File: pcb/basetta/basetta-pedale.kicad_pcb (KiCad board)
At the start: 2 copper layers, 100 x 72 mm, 33 parts, among them J1 J1, J10 J10, J2 J2, J3 J3, J4 J4, J5 J5, J6 J6, J7 J7, J8 J8, J9 J9, U1 XIAO ESP32-S3, U2 MCP23017

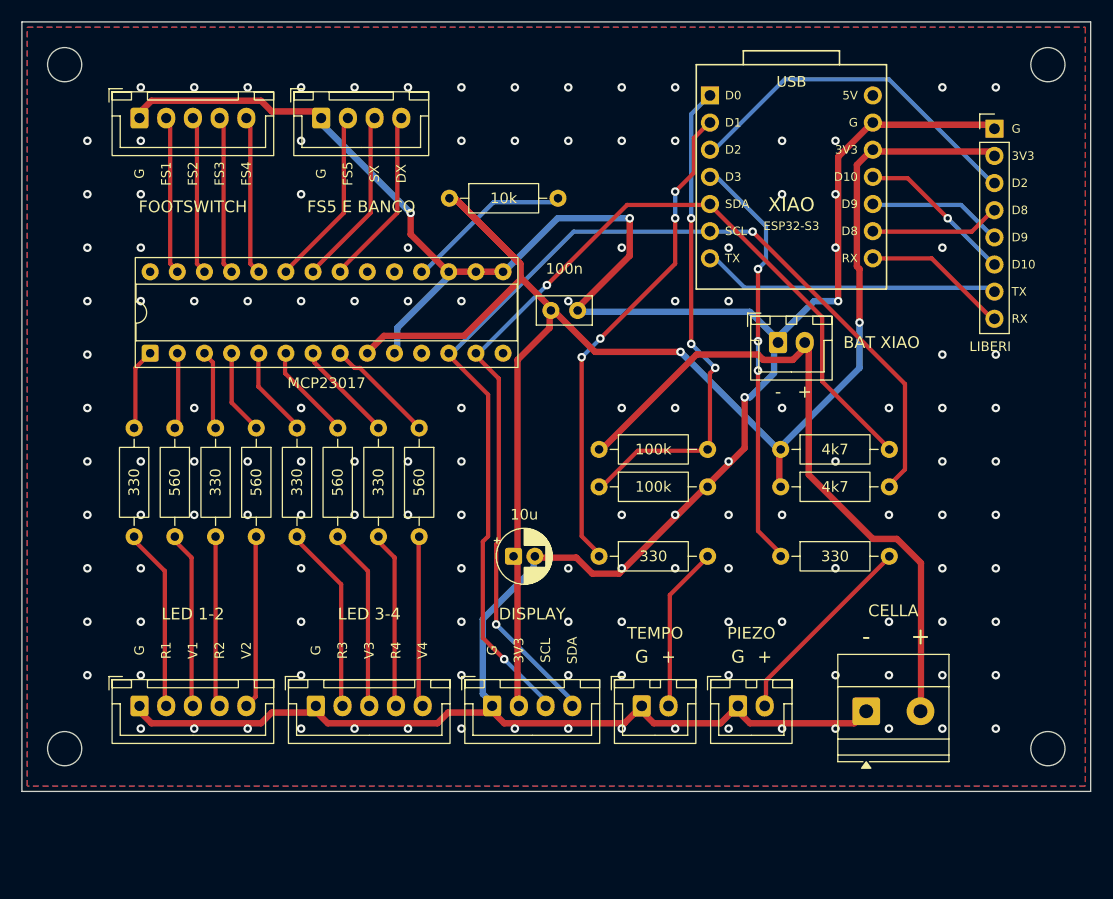
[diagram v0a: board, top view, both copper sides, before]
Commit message: Basetta: XIAO con l'USB a sinistra, logo, scheda 100 x 80
Chiesto dall'utente: la XIAO gira di 90 gradi e sta sul lato corto di
sinistra con l'USB fuori dal bordo; il logotipo in serigrafia in alto,
ricavato da icons/logo.svg (logo-serigrafia.png). Pettine LIBERI sopra la
XIAO, partitore, LED del tempo e piezo accanto ai loro piedini (D0, D1,
D3). Vie di cucitura lontane dalle piazzole e tolte se restano in un'isola.
DRC pulito.

Co-Authored-By: Claude Opus 5.5 <noreply@anthropic.com>
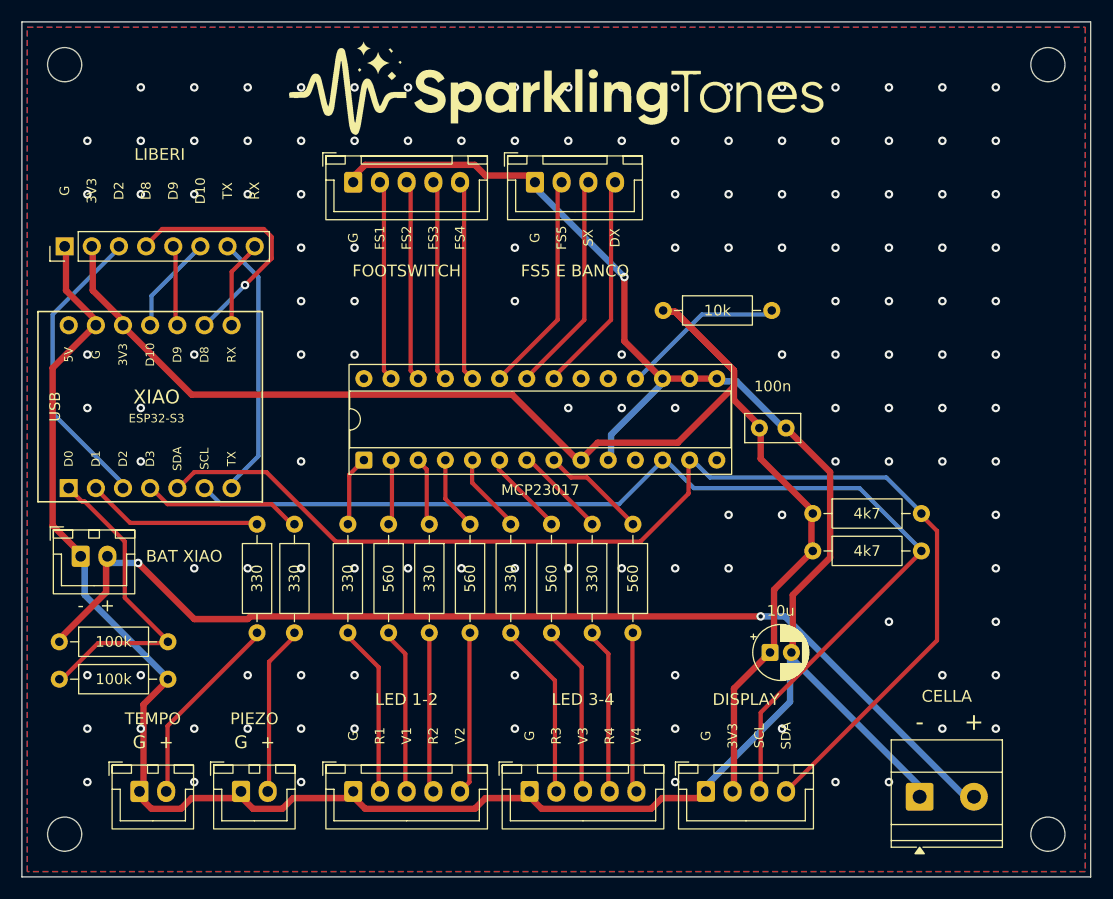
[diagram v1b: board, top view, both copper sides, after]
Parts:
- moved J10 87.7 mm to (104.0, 121.0), turned to 90 degrees
- moved J8 68.2 mm to (105.5, 150.0)
- moved U1 63.7 mm to (112.0, 136.0), turned to 90 degrees
- moved R4 53.6 mm to (103.5, 158.0)
- moved R5 53.6 mm to (103.5, 161.5)
- moved J6 47.7 mm to (111.0, 172.0)
- moved J7 47.2 mm to (120.5, 172.0)
- moved R7 45.6 mm to (125.5, 147.0), turned to -90 degrees
- moved R6 32.1 mm to (122.0, 147.0), turned to -90 degrees
- moved C2 25.6 mm to (170.0, 159.0)
- moved R3 22.6 mm to (160.0, 127.0)
- moved C1 22.4 mm to (169.0, 138.0)
- moved U2 22.4 mm to (132.0, 141.0)
- moved R12 21.9 mm to (145.7, 147.0)
- moved R10 21.9 mm to (138.1, 147.0)
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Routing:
- net VBAT: track 64.3 -> 100.5 mm, vias 0 -> 2
- net LED_T: track 46.2 -> 16.5 mm, vias 4 -> 0
- net CLIC: track 39.3 -> 14.8 mm, vias 3 -> 0
- net GND: track 263.3 -> 243.1 mm, vias 140 -> 133
- net SDA: track 94.4 -> 112.3 mm, vias 2 -> 0
- net VSENSE: track 46.6 -> 29.9 mm, vias 3 -> 0
- net +3V3: track 155.2 -> 138.6 mm, vias 2 -> 0
- net D8: track 12.2 -> 23.7 mm, vias 0 -> 1
- net RX: track 13.7 -> 8.24 mm
- net D2: track 33.3 -> 27.9 mm
- net D10: track 14.7 -> 9.28 mm, vias 1 -> 0
- net D9: track 12.6 -> 7.46 mm
- net PA5: track 14.8 -> 18.8 mm
- net PA2: track 16.7 -> 20.7 mm
- net PA3: track 14.8 -> 18.8 mm
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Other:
- board size 100 x 72 mm -> 100 x 80 mm
- board text added: "basetta del pedale v1"
- board text added: "ottobre 2026"
- board text removed: "basetta del pedale v1 - ottobre 2026"

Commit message: Basetta piu' piccola: 86 x 70, logo in verticale a destra
Chiesto dall'utente: via la fascia del logo in alto, logo piu' piccolo in
verticale nello spazio a destra con "by Massimo Togni 2026" accanto; il
morsetto della cella sul lato destro coi fili che entrano dal bordo; le
pull-up dell'I2C sdraiate sotto il condensatore. DRC pulito.

Co-Authored-By: Claude Opus 5.5 <noreply@anthropic.com>
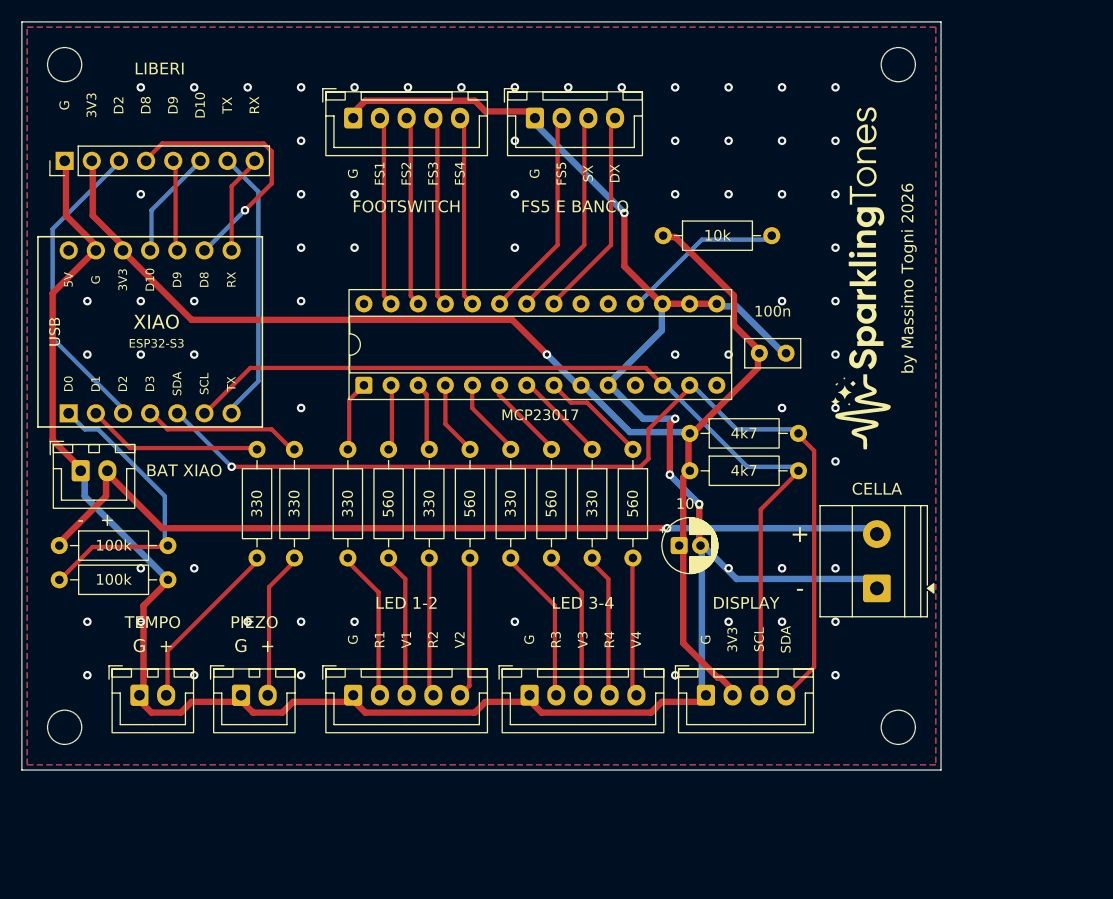
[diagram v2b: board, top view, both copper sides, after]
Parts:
- moved J9 19.9 mm to (180.0, 153.0), turned to 90 degrees
- moved H4 17.2 mm to (182.0, 166.0)
- moved H2 14.0 mm to (182.0, 104.0)
- moved R1 13.7 mm to (162.5, 138.5)
- moved R2 13.7 mm to (162.5, 142.0)
- moved C2 13.1 mm to (161.5, 149.0)
- moved H3 10.0 mm to (104.0, 166.0)
- moved R5 9.30 mm to (103.5, 152.2)
- moved J3 9.00 mm to (131.0, 163.0)
- moved J4 9.00 mm to (147.5, 163.0)
- moved J5 9.00 mm to (164.0, 163.0)
- moved J6 9.00 mm to (111.0, 163.0)
- moved J7 9.00 mm to (120.5, 163.0)
- moved R4 9.00 mm to (103.5, 149.0)
- moved J10 8.00 mm to (104.0, 113.0)
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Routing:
- net SDA: track 112.3 -> 93.1 mm, vias 0 -> 1
- net SCL: track 101.7 -> 83.8 mm
- net VBAT: track 100.5 -> 83.3 mm, vias 2 -> 1
- net +3V3: track 138.6 -> 122.3 mm, vias 0 -> 1
- net GND: track 243.1 -> 235.1 mm, vias 133 -> 71
- net LV3: track 16.0 -> 14.0 mm
- net LV2: track 15.2 -> 13.2 mm
- net LV1: track 15.5 -> 13.5 mm
- net LR4: track 15.5 -> 13.5 mm
- net LR2: track 14.9 -> 12.9 mm
- net LR1: track 16.0 -> 14.0 mm
- net LED_T_R: track 18.3 -> 16.3 mm
- net LV4: track 14.9 -> 12.9 mm
- net LR3: track 16.5 -> 14.5 mm
- net CLIC_R: track 15.8 -> 13.8 mm
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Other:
- board size 100 x 80 mm -> 86 x 70 mm
- board text added: "basetta del pedale v1 - ottobre 2026"
- board text added: "by Massimo Togni 2026"
- board text removed: "SPARKLINGTONES"
- board text removed: "basetta del pedale v1"
- board text removed: "ottobre 2026"

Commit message: Basetta: la presa del pedale d'espressione (J11)
JST-XH a 4 poli in alto a destra, G, 3V3, D2, D8: lo stesso ordine della presa
H della millefori, cosi' il cavo fatto entra uguale. Resistenza e condensatore
restano sulla presa del pedale (scelta dell'utente). La 10k del RESET scende
di 3 mm. Verifica: 119 piazzole, 0 errori; DRC pulito; Gerber e zip rifatti.

Co-Authored-By: Claude Opus 5.5 <noreply@anthropic.com>
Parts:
- added J11: J11, JST_XH_B4B-XH-A_1x04_P2.50mm_Vertical, F.Cu at (163.0, 109.0)
- moved R3 3.00 mm to (160.0, 123.0)
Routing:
- net D2: track 28.9 -> 89.9 mm
- net D8: track 24.7 -> 85.6 mm
- net +3V3: track 122.3 -> 137.2 mm, vias 1 -> 0
- net GND: track 235.1 -> 249.0 mm, vias 71 -> 55
- net SDA: track 93.1 -> 91.4 mm, vias 1 -> 2
- net RESET: track 15.4 -> 14.2 mm
- net TX: track 25.9 -> 25.0 mm, vias 0 -> 1
- net SCL: vias 0 -> 1
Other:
- board text added: "ESPRESSIONE"

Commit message: Basetta: piazzole BAT sotto la XIAO e «pedal» sotto il logo
La presa BAT XIAO lascia il posto a due piazzole fra le file della XIAO,
collegate come prima (morsetto e partitore): due fili corti nascosti sotto
la XIAO. Sotto il logo la scritta «pedal». Verifica 119 piazzole, 0 errori;
DRC pulito; Gerber, zip e anteprime rifatti.

Co-Authored-By: Claude Opus 5.5 <noreply@anthropic.com>
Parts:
- J8: value J8 -> BAT; footprint JST_XH_B2B-XH-A_1x02_P2.50mm_Vertical -> (none)
- moved J8 17.7 mm to (117.5, 129.0)
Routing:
- net VBAT: track 83.3 -> 105.5 mm, vias 1 -> 2
- net GND: track 249.0 -> 264.6 mm, vias 55 -> 61
- net SDA: track 91.4 -> 89.6 mm, vias 2 -> 1
- net VSENSE: track 28.4 -> 27.7 mm
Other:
- board text added: "BAT"
- board text added: "pedal"
- board text removed: "BAT XIAO"
